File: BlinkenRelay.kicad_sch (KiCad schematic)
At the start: 21 parts, among them J1 Conn_02x07_Odd_Even, J2 Conn_01x08_Pin, J3 Conn_01x08_Socket, SW1 SW_DIP_x01, U1 LTV-817, U2 LTV-817, U3 LTV-817, U4 LTV-817, U5 LTV-817, U6 LTV-817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

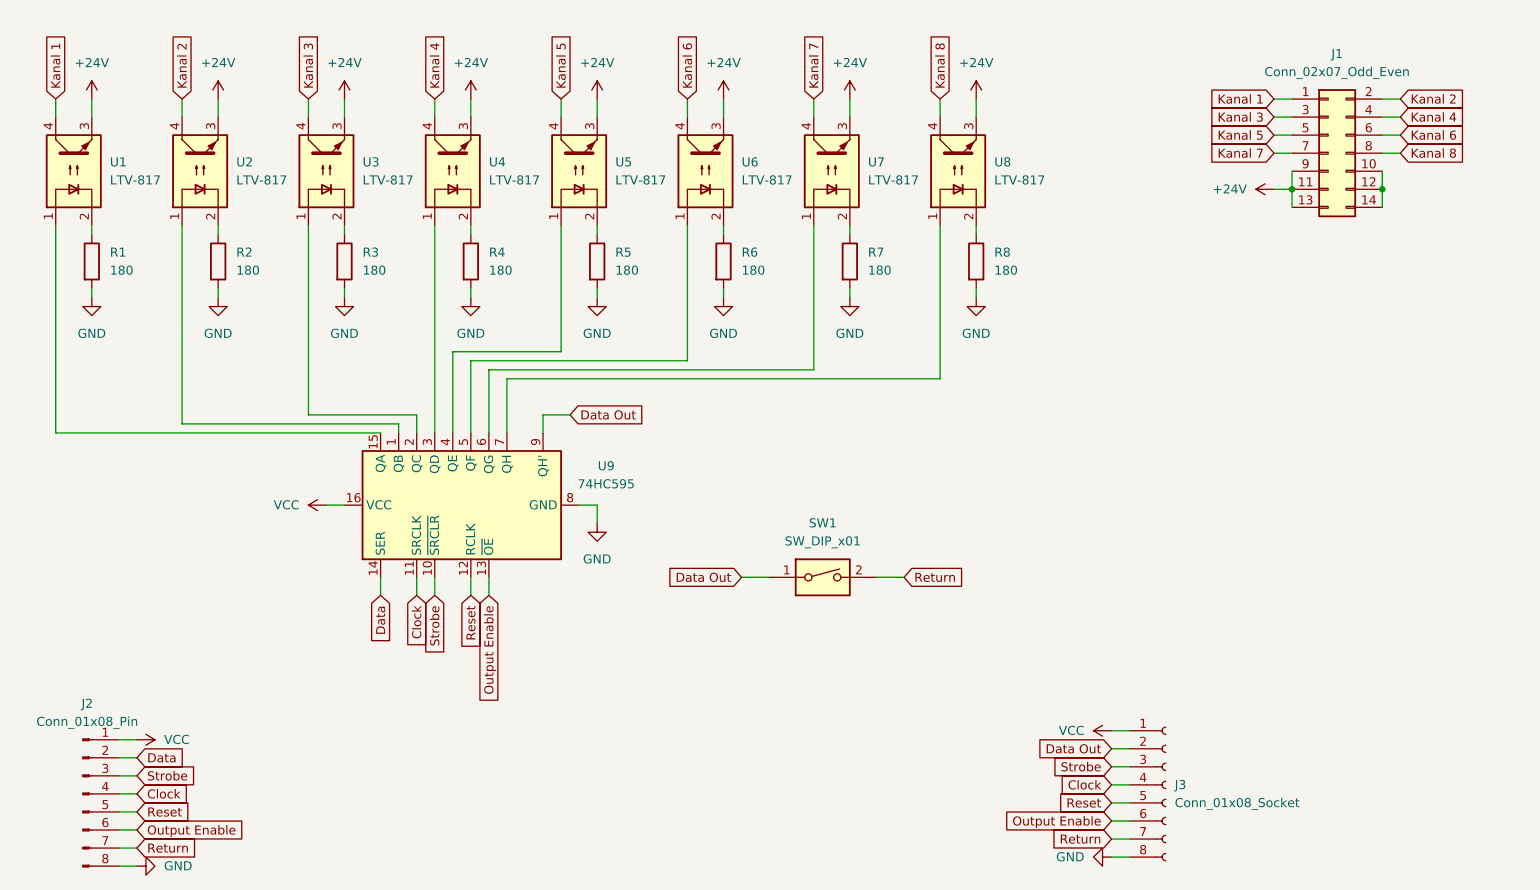
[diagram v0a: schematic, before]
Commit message: New revision. Fixed switched Pins.
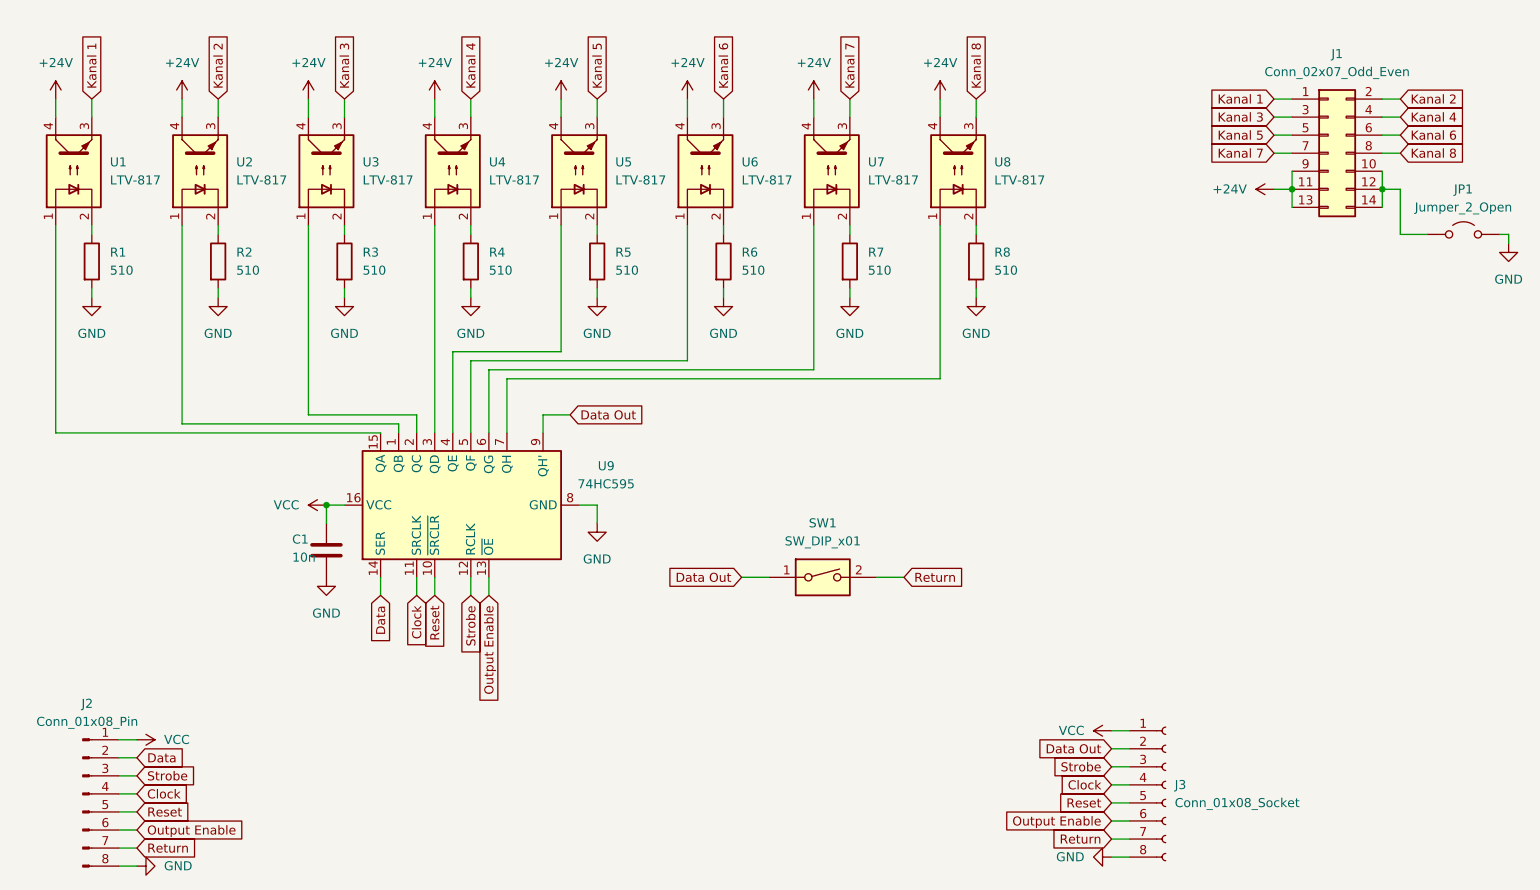
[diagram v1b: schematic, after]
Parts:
- added C1: 10n, Capacitor_THT:C_Disc_D5.0mm_W2.5mm_P5.00mm, symbol Device:C
- added JP1: Jumper_2_Open, Jumper:SolderJumper-2_P1.3mm_Open_Pad1.0x1.5mm, symbol Jumper:Jumper_2_Open
- J1: footprint Connector_IDC:IDC-Header_2x07_P2.54mm_Vertical -> Connector_IDC:IDC-Header_2x07_P2.54mm_Latch_Vertical
- J2: footprint Connector_PinHeader_2.54mm:PinHeader_1x08_P2.54mm_Vertical -> Connector_PinHeader_2.54mm:PinHeader_1x08_P2.54mm_Horizontal
- R1, R2, R3, R4, R5, R6, R7, R8: value 180 -> 510; footprint Resistor_THT:R_Axial_DIN0204_L3.6mm_D1.6mm_P5.08mm_Horizontal -> Resistor_THT:R_Axial_DIN0309_L9.0mm_D3.2mm_P5.08mm_Vertical
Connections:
- net +24V: now also U1.4, U2.4, U3.4, U4.4, U5.4, U6.4, U7.4, U8.4; no longer U1.3, U2.3, U3.3, U4.3, U5.3, U6.3, U7.3, U8.3
- net GND: now also C1.2, JP1.2 (B)
- net Kanal 1: now also U1.3; no longer U1.4
- net Kanal 2: now also U2.3; no longer U2.4
- net Kanal 3: now also U3.3; no longer U3.4
- net Kanal 4: now also U4.3; no longer U4.4
- net Kanal 5: now also U5.3; no longer U5.4
- net Kanal 6: now also U6.3; no longer U6.4
- net Kanal 7: now also U7.3; no longer U7.4
- net Kanal 8: now also U8.3; no longer U8.4
- net Reset: now also U9.10 (~{SRCLR}); no longer U9.12 (RCLK)
- net Strobe: now also U9.12 (RCLK); no longer U9.10 (~{SRCLR})
- net VCC: now also C1.1
- net at J1.10 (Pin_10), J1.12 (Pin_12), J1.14 (Pin_14): now also JP1.1 (A)

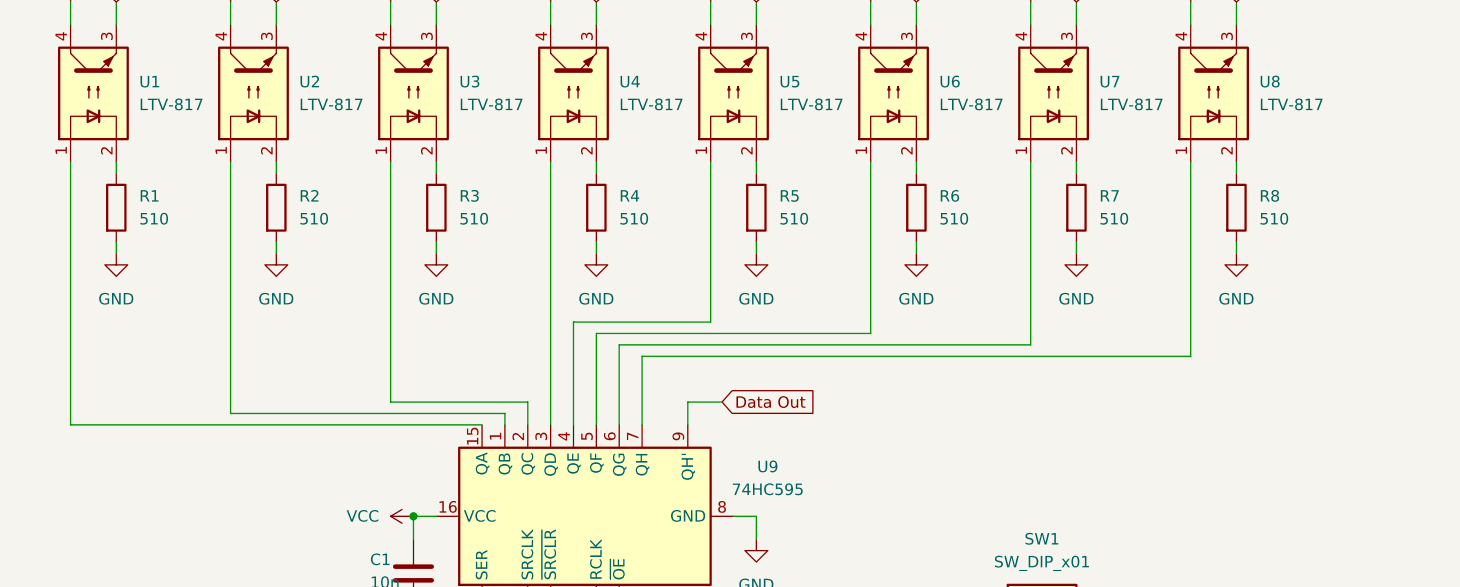
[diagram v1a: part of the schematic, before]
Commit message: Added status LEDS and removed backups from git.
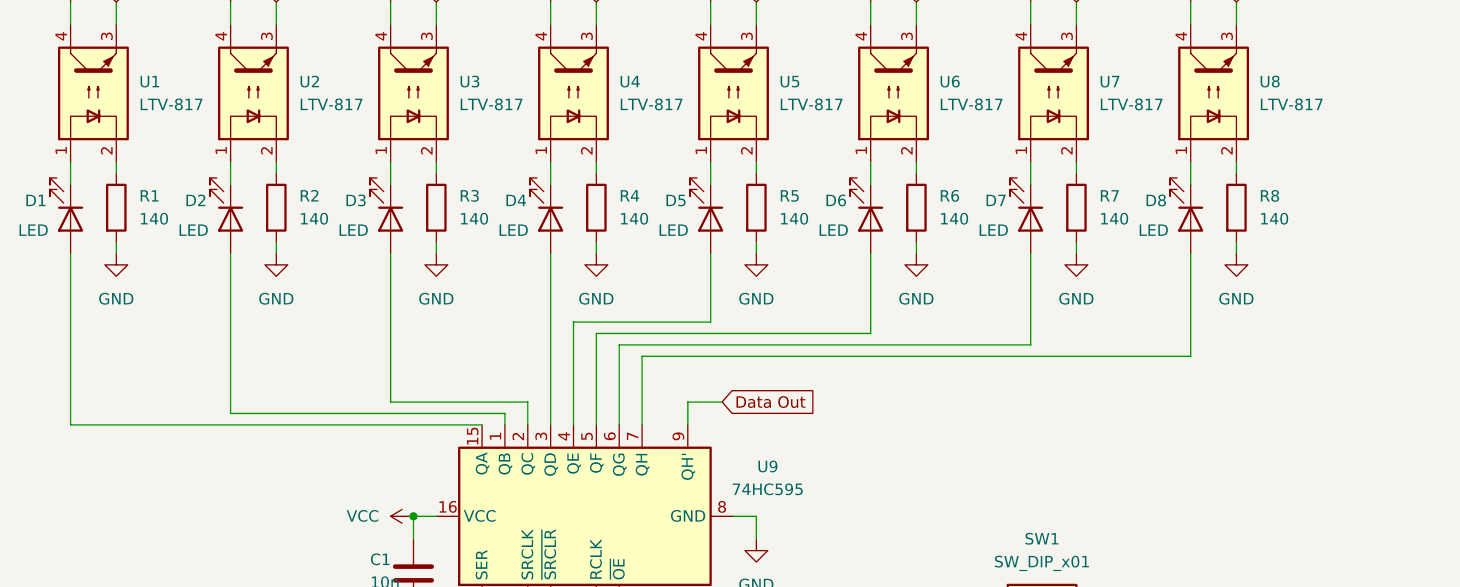
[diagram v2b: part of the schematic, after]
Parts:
- added D1, D2, D3, D4, D5, D6, D7, D8: LED, LED_THT:LED_D3.0mm, symbol Device:LED
- R1, R2, R3, R4, R5, R6, R7, R8: value 510 -> 140
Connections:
- net at U1.1: now also D1.1 (K); no longer U9.15 (QA)
- net at U2.1: now also D2.1 (K); no longer U9.1 (QB)
- net at U3.1: now also D3.1 (K); no longer U9.2 (QC)
- net at U4.1: now also D4.1 (K); no longer U9.3 (QD)
- net at U5.1: now also D5.1 (K); no longer U9.4 (QE)
- net at U6.1: now also D6.1 (K); no longer U9.5 (QF)
- net at U8.1: now also D8.1 (K); no longer U9.7 (QH)
- net at U7.1: now also D7.1 (K); no longer U9.6 (QG)
- new net: D6.2 (A), U9.5 (QF)
- new net: D5.2 (A), U9.4 (QE)
- new net: D1.2 (A), U9.15 (QA)
- new net: D3.2 (A), U9.2 (QC)
- new net: D8.2 (A), U9.7 (QH)
- new net: D7.2 (A), U9.6 (QG)
- new net: D2.2 (A), U9.1 (QB)
- new net: D4.2 (A), U9.3 (QD)
